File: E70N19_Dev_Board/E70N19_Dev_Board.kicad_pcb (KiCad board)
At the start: 2 copper layers, 100 x 100 mm, 77 parts, among them J1 USB_microB_2040002-1, J2 Battery 1x2, J3 JTAGSEL_JUMPER 1x3, J4 UART_PROG 1x2, J5 ERASE_JUMPER 1x3, J6 ARM-Cortex-Debug-10, J7 CAN 1x2, J8 Conn_02x15_Counter_Clockwise, J9 Conn_02x15_Counter_Clockwise, SW1 NRST_BUTTON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

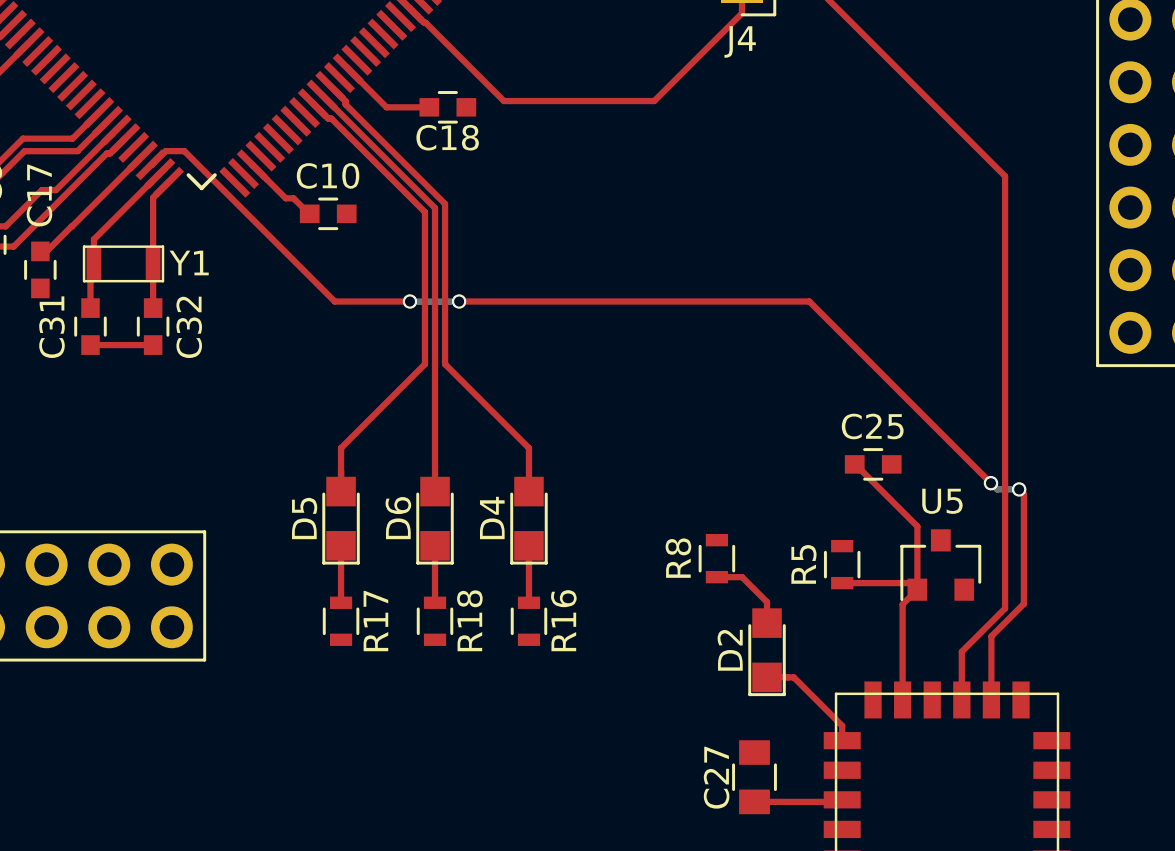
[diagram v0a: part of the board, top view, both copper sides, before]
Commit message: Primary four layer fanout
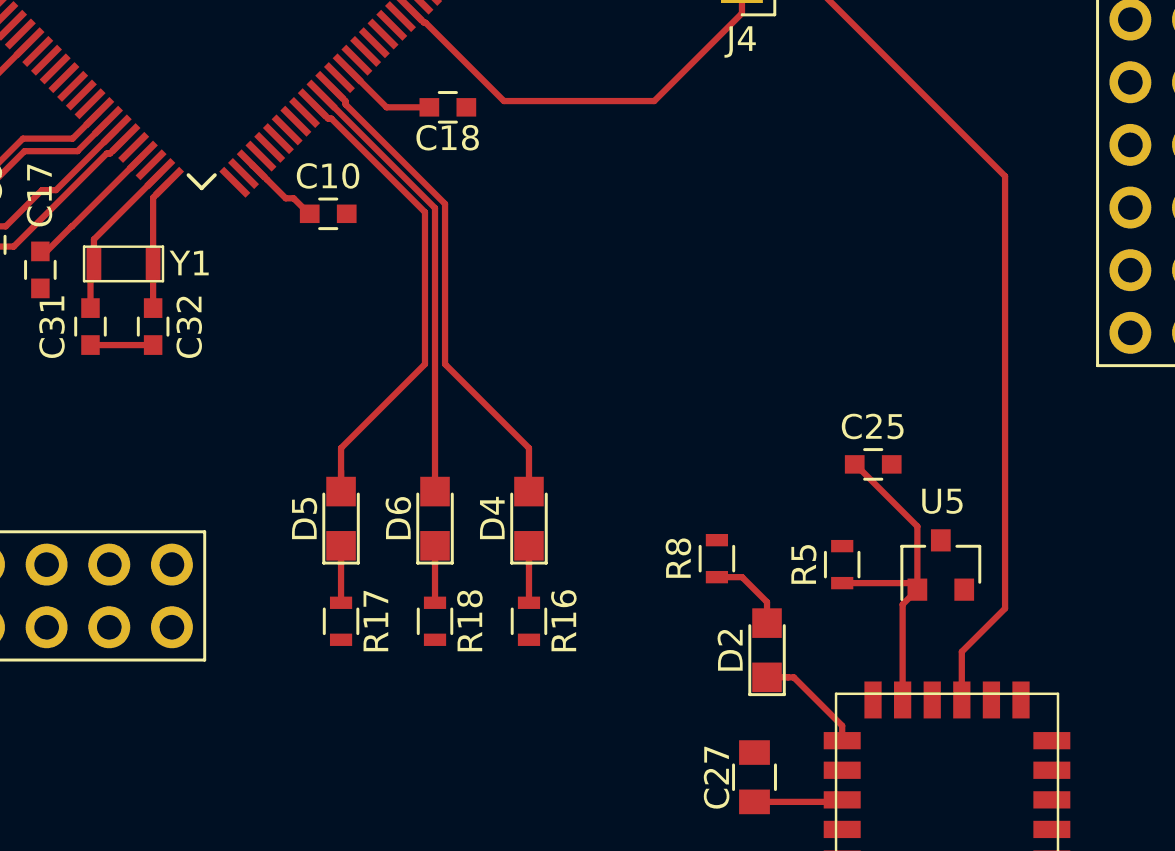
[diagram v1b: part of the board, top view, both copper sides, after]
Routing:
- net Net-(FP1-Pad7): track 50.3 -> 0.00 mm, vias 4 -> 0
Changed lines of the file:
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@@
-(kicad_pcb (version 4) (host pcbnew 4.0.7)
+(kicad_pcb (version 4) (host pcbnew 4.0.2+dfsg1-stable)
   (general
     (links 241)
-    (no_connects 231)
-    (area 80.264999 25.324999 187.245735 125.475001)
+    (no_connects 152)
+    (area 81.49 24.2006 183.641001 125.475001)
     (thickness 1.6)
     (drawings 4)
-    (tracks 373)
+    (tracks 355)
     (zones 0)
     (modules 77)
@@
   )
   (setup
-    (last_trace_width 0.254)
+    (last_trace_width 0.2032)
     (user_trace_width 0.254)
     (user_trace_width 0.508)
@@
     (add_net "Net-(U4-Pad74)")
   )
+  (module eclectronics:BM71BLES1FC2 (layer F.Cu)
+    (at 163.69 101.25 180)
+    (fp_text reference FP1 (at 1.778 -14.01572 180) (layer F.SilkS)
+      (effects (font (size 1 1) (thickness 0.15)))
+    )
+    (fp_text value BM71BLES1FC2 (at 4.32816 -12.5222 180) (layer F.Fab)
+      (effects (font (size 1 1) (thickness 0.15)))
+    )
+    (fp_line (start 0 -7.5) (end 9 -7.5) (layer F.SilkS) (width 0.1))
+    (fp_arc (start 9 -9.6) (end 9 -9.2) (angle 180) (layer F.SilkS) (width 0.1))
+    (fp_line (start 0 -11.5) (end 9 -11.5) (layer F.SilkS) (width 0.1))
+    (fp_line (start 0 0) (end 0 -11.5) (layer F.SilkS) (width 0.1))
+    (fp_line (start 9 0) (end 9 -11.5) (layer F.SilkS) (width 0.1))
+    (fp_line (start 0 0) (end 9 0) (layer F.SilkS) (width 0.1))
+    (pad 6 smd rect (at 1.5 -0.25 180) (size 0.7 1.5) (layers F.Cu F.Paste F.Mask)
+      (net 19 "Net-(FP1-Pad6)"))
+    (pad 7 smd rect (at 2.7 -0.25 180) (size 0.7 1.5) (layers F.Cu F.Paste F.Mask)
+      (net 20 "Net-(FP1-Pad7)"))
+    (pad 8 smd rect (at 3.9 -0.25 180) (size 0.7 1.5) (layers F.Cu F.Paste F.Mask)
+      (net 21 "Net-(FP1-Pad8)"))
+    (pad 9 smd rect (at 5.1 -0.25 180) (size 0.7 1.5) (layers F.Cu F.Paste F.Mask)
+      (net 22 "Net-(FP1-Pad9)"))
+    (pad 10 smd rect (at 6.3 -0.25 180) (size 0.7 1.5) (layers F.Cu F.Paste F.Mask)
+      (net 10 "Net-(C25-Pad1)"))
+    (pad 11 smd rect (at 7.5 -0.25 180) (size 0.7 1.5) (layers F.Cu F.Paste F.Mask)
+      (net 23 "Net-(FP1-Pad11)"))
+    (pad 5 smd rect (at 0.25 -1.9 90) (size 0.7 1.5) (layers F.Cu F.Paste F.Mask)
+      (net 24 "Net-(FP1-Pad5)"))
+    (pad 4 smd rect (at 0.25 -3.1 90) (size 0.7 1.5) (layers F.Cu F.Paste F.Mask)
+      (net 25 "Net-(FP1-Pad4)"))
+    (pad 3 smd rect (at 0.25 -4.3 90) (size 0.7 1.5) (layers F.Cu F.Paste F.Mask)
+      (net 26 "Net-(FP1-Pad3)"))
+    (pad 2 smd rect (at 0.25 -5.5 90) (size 0.7 1.5) (layers F.Cu F.Paste F.Mask)
+      (net 1 GND))
+    (pad 1 smd rect (at 0.25 -6.7 90) (size 0.7 1.5) (layers F.Cu F.Paste F.Mask)
+      (net 27 "Net-(FP1-Pad1)"))
+    (pad 12 smd rect (at 8.75 -1.9 90) (size 0.7 1.5) (layers F.Cu F.Paste F.Mask)
+      (net 17 "Net-(D2-Pad1)"))
+    (pad 13 smd rect (at 8.75 -3.1 90) (size 0.7 1.5) (layers F.Cu F.Paste F.Mask)
+      (net 1 GND))
+    (pad 14 smd rect (at 8.75 -4.3 90) (size 0.7 1.5) (layers F.Cu F.Paste F.Mask)
+      (net 3 +3V3))
+    (pad 15 smd rect (at 8.75 -5.5 90) (size 0.7 1.5) (layers F.Cu F.Paste F.Mask)
+      (net 28 "Net-(FP1-Pad15)"))
+    (pad 16 smd rect (at 8.75 -6.7 90) (size 0.7 1.5) (layers F.Cu F.Paste F.Mask)
+      (net 29 "Net-(FP1-Pad16)"))
+  )
   (module Capacitors_SMD:C_0603 (layer F.Cu)
     (at 93.98 41.898 270)
@@
     )
   )
-  (module eclectronics:BM71BLES1FC2 (layer F.Cu)
-    (at 163.69 101.25 180)
-    (fp_text reference FP1 (at 1.778 -14.01572 180) (layer F.SilkS)
-      (effects (font (size 1 1) (thickness 0.15)))
-    )
-    (fp_text value BM71BLES1FC2 (at 4.32816 -12.5222 180) (layer F.Fab)
-      (effects (font (size 1 1) (thickness 0.15)))
-    )
-    (fp_line (start 0 -7.5) (end 9 -7.5) (layer F.SilkS) (width 0.1))
-    (fp_arc (start 9 -9.6) (end 9 -9.2) (angle 180) (layer F.SilkS) (width 0.1))
-    (fp_line (start 0 -11.5) (end 9 -11.5) (layer F.SilkS) (width 0.1))
-    (fp_line (start 0 0) (end 0 -11.5) (layer F.SilkS) (width 0.1))
-    (fp_line (start 9 0) (end 9 -11.5) (layer F.SilkS) (width 0.1))
-    (fp_line (start 0 0) (end 9 0) (layer F.SilkS) (width 0.1))
-    (pad 6 smd rect (at 1.5 -0.25 180) (size 0.7 1.5) (layers F.Cu F.Paste F.Mask)
-      (net 19 "Net-(FP1-Pad6)"))
-    (pad 7 smd rect (at 2.7 -0.25 180) (size 0.7 1.5) (layers F.Cu F.Paste F.Mask)
-      (net 20 "Net-(FP1-Pad7)"))
-    (pad 8 smd rect (at 3.9 -0.25 180) (size 0.7 1.5) (layers F.Cu F.Paste F.Mask)
-      (net 21 "Net-(FP1-Pad8)"))
-    (pad 9 smd rect (at 5.1 -0.25 180) (size 0.7 1.5) (layers F.Cu F.Paste F.Mask)
-      (net 22 "Net-(FP1-Pad9)"))
-    (pad 10 smd rect (at 6.3 -0.25 180) (size 0.7 1.5) (layers F.Cu F.Paste F.Mask)
-      (net 10 "Net-(C25-Pad1)"))
-    (pad 11 smd rect (at 7.5 -0.25 180) (size 0.7 1.5) (layers F.Cu F.Paste F.Mask)
-      (net 23 "Net-(FP1-Pad11)"))
-    (pad 5 smd rect (at 0.25 -1.9 90) (size 0.7 1.5) (layers F.Cu F.Paste F.Mask)
-      (net 24 "Net-(FP1-Pad5)"))
-    (pad 4 smd rect (at 0.25 -3.1 90) (size 0.7 1.5) (layers F.Cu F.Paste F.Mask)
-      (net 25 "Net-(FP1-Pad4)"))
-    (pad 3 smd rect (at 0.25 -4.3 90) (size 0.7 1.5) (layers F.Cu F.Paste F.Mask)
-      (net 26 "Net-(FP1-Pad3)"))
-    (pad 2 smd rect (at 0.25 -5.5 90) (size 0.7 1.5) (layers F.Cu F.Paste F.Mask)
-      (net 1 GND))
-    (pad 1 smd rect (at 0.25 -6.7 90) (size 0.7 1.5) (layers F.Cu F.Paste F.Mask)
-      (net 27 "Net-(FP1-Pad1)"))
-    (pad 12 smd rect (at 8.75 -1.9 90) (size 0.7 1.5) (layers F.Cu F.Paste F.Mask)
-      (net 17 "Net-(D2-Pad1)"))
-    (pad 13 smd rect (at 8.75 -3.1 90) (size 0.7 1.5) (layers F.Cu F.Paste F.Mask)
-      (net 1 GND))
-    (pad 14 smd rect (at 8.75 -4.3 90) (size 0.7 1.5) (layers F.Cu F.Paste F.Mask)
-      (net 3 +3V3))
-    (pad 15 smd rect (at 8.75 -5.5 90) (size 0.7 1.5) (layers F.Cu F.Paste F.Mask)
-      (net 28 "Net-(FP1-Pad15)"))
-    (pad 16 smd rect (at 8.75 -6.7 90) (size 0.7 1.5) (layers F.Cu F.Paste F.Mask)
-      (net 29 "Net-(FP1-Pad16)"))
-  )
   (module eclectronics:USB_microB_2040002-1 (layer F.Cu)
     (at 85.1074 52.227 270)
@@
   (segment (start 152.746 100.584) (end 151.892 100.584) (width 0.254) (layer F.Cu) (net 17))
   (segment (start 123.104 43.18) (end 124.992 43.18) (width 0.254) (layer F.Cu) (net 18))
-  (segment (start 127.510518 79.245482) (end 126.955337 79.800663) (width 0.254) (layer F.Cu) (net 20))
-  (segment (start 126.955337 79.800663) (end 126.918125 79.800663) (width 0.254) (layer F.Cu) (net 20))
-  (segment (start 134.366 85.344) (end 128.267482 79.245482) (width 0.254) (layer F.Cu) (net 20))
-  (segment (start 128.267482 79.245482) (end 127.510518 79.245482) (width 0.254) (layer F.Cu) (net 20))
-  (segment (start 137.414 85.344) (end 134.366 85.344) (width 0.254) (layer F.Cu) (net 20))
-  (segment (start 139.40791 85.344) (end 137.414 85.344) (width 0.254) (layer B.Cu) (net 20))
-  (via (at 137.414 85.344) (size 0.5842) (drill 0.4064) (layers F.Cu B.Cu) (net 20))
-  (segment (start 153.6065 85.344) (end 139.40791 85.344) (width 0.254) (layer F.Cu) (net 20))
-  (via (at 139.40791 85.344) (size 0.5842) (drill 0.4064) (layers F.Cu B.Cu) (net 20))
-  (segment (start 160.9725 92.71) (end 153.6065 85.344) (width 0.254) (layer F.Cu) (net 20))
-  (segment (start 162.1155 92.964) (end 161.2265 92.964) (width 0.254) (layer B.Cu) (net 20))
-  (segment (start 161.2265 92.964) (end 160.9725 92.71) (width 0.254) (layer B.Cu) (net 20))
-  (via (at 160.9725 92.71) (size 0.5842) (drill 0.4064) (layers F.Cu B.Cu) (net 20))
-  (segment (start 162.306 97.60275) (end 162.306 93.1545) (width 0.254) (layer F.Cu) (net 20))
-  (segment (start 162.306 93.1545) (end 162.1155 92.964) (width 0.254) (layer F.Cu) (net 20))
-  (via (at 162.1155 92.964) (size 0.5842) (drill 0.4064) (layers F.Cu B.Cu) (net 20))
-  (segment (start 160.99 101.5) (end 160.99 98.91875) (width 0.254) (layer F.Cu) (net 20))
-  (segment (start 160.99 98.91875) (end 162.306 97.60275) (width 0.254) (layer F.Cu) (net 20))
   (segment (start 141.732 66.802) (end 141.331002 66.802) (width 0.254) (layer F.Cu) (net 21))
   (segment (start 141.331002 66.802) (end 138.797519 69.335483) (width 0.254) (layer F.Cu) (net 21))

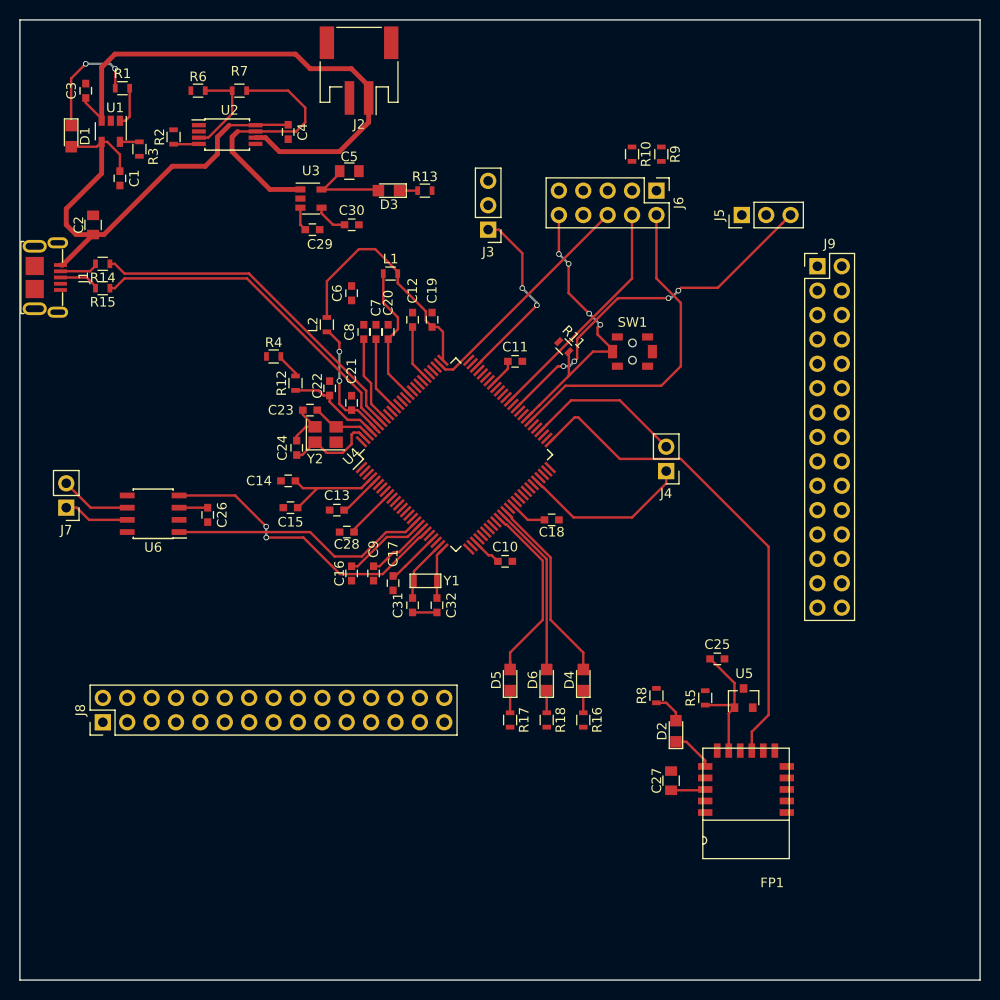
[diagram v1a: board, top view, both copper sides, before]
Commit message: Fixed up fanout connections
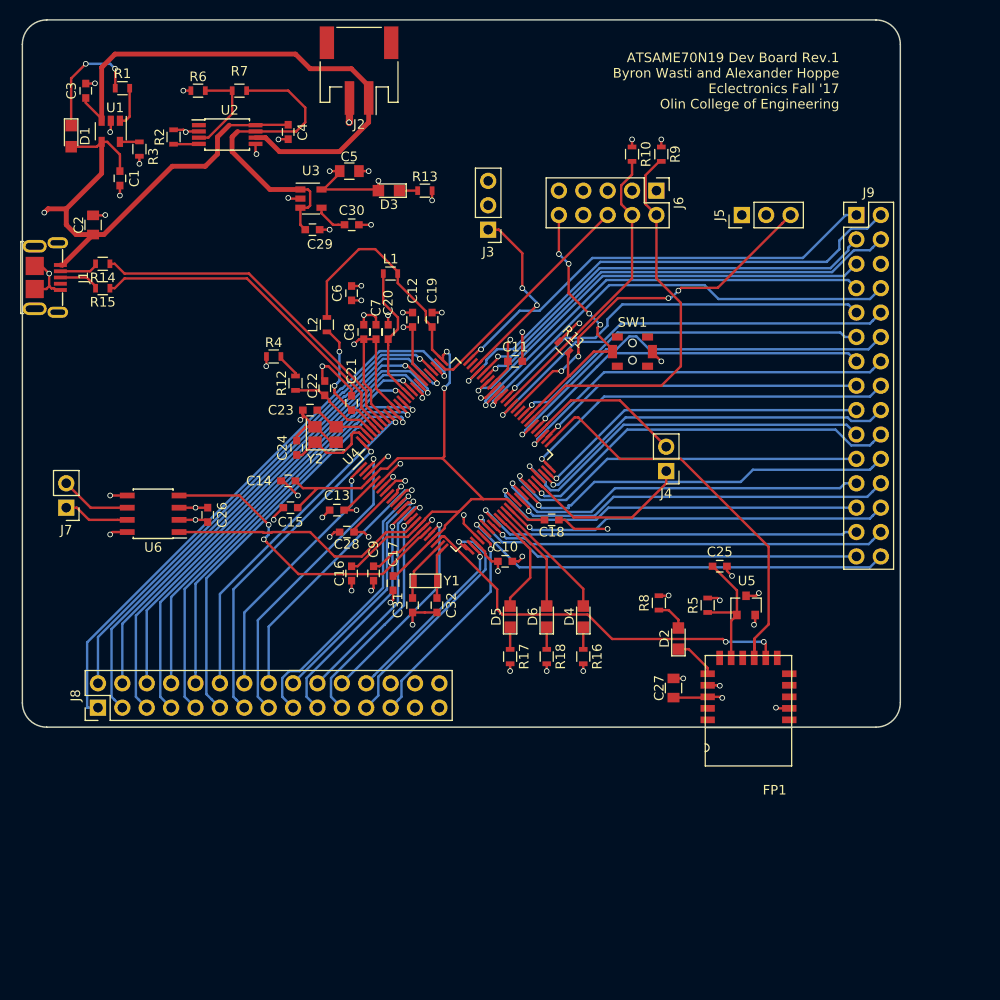
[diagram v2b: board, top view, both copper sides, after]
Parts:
- moved C27 9.66 mm to (151.6, 95.0)
- moved D2 9.66 mm to (152.1, 89.8)
- moved FP1 9.66 mm to (163.9, 91.6)
- moved R5 9.66 mm to (155.2, 86.4)
- moved R8 9.66 mm to (150.1, 86.1)
- moved U5 9.66 mm to (159.2, 86.4)
- moved C25 9.66 mm to (156.5, 82.3)
- moved J9 6.71 mm to (170.7, 45.7)
- moved D4 6.60 mm to (142.2, 87.5)
- moved D5 6.60 mm to (134.6, 87.5)
- moved D6 6.60 mm to (138.4, 87.5)
- moved R16 6.60 mm to (142.2, 91.7)
- moved R17 6.60 mm to (134.6, 91.7)
- moved R18 6.60 mm to (138.4, 91.7)
- moved J8 1.61 mm to (91.7, 97.0)
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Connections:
- J8 pad 1: /PD0 -> /PD9
- J8 pad 10: /PD9 -> /PD3
- J8 pad 11: /PD10 -> /PD2
- J8 pad 12: /PD11 -> /PD1
- J8 pad 13: /PD12 -> /PB13
- J8 pad 14: /PD13 -> /PD0
- J8 pad 15: /PD14 -> /PD31
- J8 pad 16: /PD15 -> /PB1
- J8 pad 17: /PD16 -> /PB0
- J8 pad 18: /PD17 -> /PA20
- J8 pad 19: /PD18 -> /PA19
- J8 pad 2: /PD1 -> /PA28
- J8 pad 20: /PD19 -> /PA18
- J8 pad 21: /PD20 -> /PA17
- J8 pad 22: /PD21 -> /PA21
- J8 pad 23: /PD22 -> /PA22
- J8 pad 24: /PD27 -> /PA13
- J8 pad 25: /PD31 -> /PA16
- J8 pad 3: /PD2 -> /PD8
- J8 pad 4: /PD3 -> /PA30
- J8 pad 5: /PD4 -> /PA31
- J8 pad 6: /PD5 -> /PD7
- J8 pad 8: /PD7 -> /PD5
- J8 pad 9: /PD8 -> /PD4
- J9 pad 1: /PA0 -> /PD15
- J9 pad 10: /PA14 -> /PD13
- J9 pad 11: /PA15 -> /PD14
- J9 pad 12: /PA16 -> /PD16
- J9 pad 13: /PA17 -> /PA4
- J9 pad 14: /PA18 -> /PD17
- J9 pad 15: /PA19 -> GND
- J9 pad 16: /PA20 -> /PA27
- J9 pad 17: /PA21 -> /PD18
- J9 pad 18: /PA22 -> /PA12
- J9 pad 19: /PA23 -> /PD19
- J9 pad 2: /PA1 -> /PA0
- J9 pad 20: /PA24 -> /PD20
- J9 pad 21: /PA25 -> /PA11
- J9 pad 22: /PA26 -> /PD21
- J9 pad 23: /PA27 -> /PA26
- J9 pad 24: /PA28 -> /PD22
- J9 pad 25: /PA30 -> /PA25
- J9 pad 26: /PA31 -> /PA24
- J9 pad 27: /PB0 -> /PA14
- J9 pad 28: /PB1 -> /PA15
- J9 pad 29: /PB13 -> /PD27
- J9 pad 3: /PA2 -> /PD10
- J9 pad 30: Net-(J9-Pad30) -> /PA23
- J9 pad 4: /PA3 -> /PA1
- J9 pad 5: /PA4 -> /PD11
- J9 pad 7: /PA11 -> /PA2
- J9 pad 8: /PA12 -> /PD12
- J9 pad 9: /PA13 -> /PA3
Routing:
- net GND: track 7.59 -> 138.8 mm, vias 0 -> 55
- net /VBUS: track 51.9 -> 148.0 mm, vias 0 -> 1
- net /PD9: track 0.00 -> 60.3 mm, vias 0 -> 1
- net /PD8: track 0.00 -> 56.6 mm, vias 0 -> 1
- net /PA31: track 0.00 -> 53.5 mm, vias 0 -> 1
- net /PA28: track 0.00 -> 52.5 mm, vias 0 -> 1
- net /PA0: track 0.00 -> 52.3 mm, vias 0 -> 1
- net /PD12: track 0.00 -> 50.0 mm, vias 0 -> 1
- net /PA30: track 0.00 -> 49.2 mm, vias 0 -> 1
- net /PD7: track 0.00 -> 49.2 mm, vias 0 -> 1
- net /PD6: track 0.00 -> 47.8 mm, vias 0 -> 1
- net /PA1: track 0.00 -> 47.1 mm, vias 0 -> 1
- net /PA2: track 0.00 -> 46.7 mm, vias 0 -> 1
- net /PD15: track 0.00 -> 46.6 mm, vias 0 -> 1
- net /PD11: track 0.00 -> 46.4 mm, vias 0 -> 1
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- added copper zone on In2.Cu, net +3V3
- added copper zone on In1.Cu, net GND
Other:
- board size 100 x 100 mm -> 91.4 x 73.7 mm
- copper layers 2 -> 4
- board text added: "ATSAME70N19 Dev Board Rev.1 Byron Wasti and Alexander Hoppe Eclectronics Fall '17 Olin College of Engineering"
